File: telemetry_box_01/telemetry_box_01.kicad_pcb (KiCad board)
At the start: 4 copper layers, 86 x 44 mm, 103 parts, among them J1 78646-3001, J2 U.FL-R-SMT-1_10_, J3 U.FL-R-SMT-1_10_, J4 12401832E402A, U1 nRF52840, U2 A9G, U3 STBC08PMR, U4 TPS7A2633DRVR, Y1 Crystal_GND24, Y2 ABS04W-32.768KHZ-4-D2-T5

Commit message: fix(vias): blind vias have been removed to optimize production
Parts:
- C11, C12: value 0.8 -> 12
- C13, C14: value 0.8 -> 2
- R6, R7, R8, R9: value 1k -> 510
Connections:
- U1 pad A10: unconnected-(U1-AIN5/P0.29-PadA10) -> NRF_GPIO_01
- U1 pad A8: unconnected-(U1-AIN7/P0.31-PadA8) -> NRF_GPIO_02
- U1 pad AC15: unconnected-(U1-P0.19-PadAC15) -> NRF_RESET
- U1 pad AC17: unconnected-(U1-P0.21-PadAC17) -> NRF_RESET
- U1 pad AC19: unconnected-(U1-P0.23-PadAC19) -> NRF_RESET
- U1 pad AC21: unconnected-(U1-P0.25-PadAC21) -> NRF_RESET
- U1 pad B11: NRF_GPIO_01 -> unconnected-(U1-AIN4/P0.28-PadB11)
- U1 pad B9: NRF_GPIO_02 -> unconnected-(U1-AIN6/P0.30-PadB9)
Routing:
- net NRF_RESET: track 28.2 -> 29.8 mm, vias 4 -> 3
- net NRF_GPIO_02: track 9.54 -> 9.11 mm, vias 3 -> 2
- net NRF_GPIO_01: track 13.6 -> 13.2 mm, vias 3 -> 2

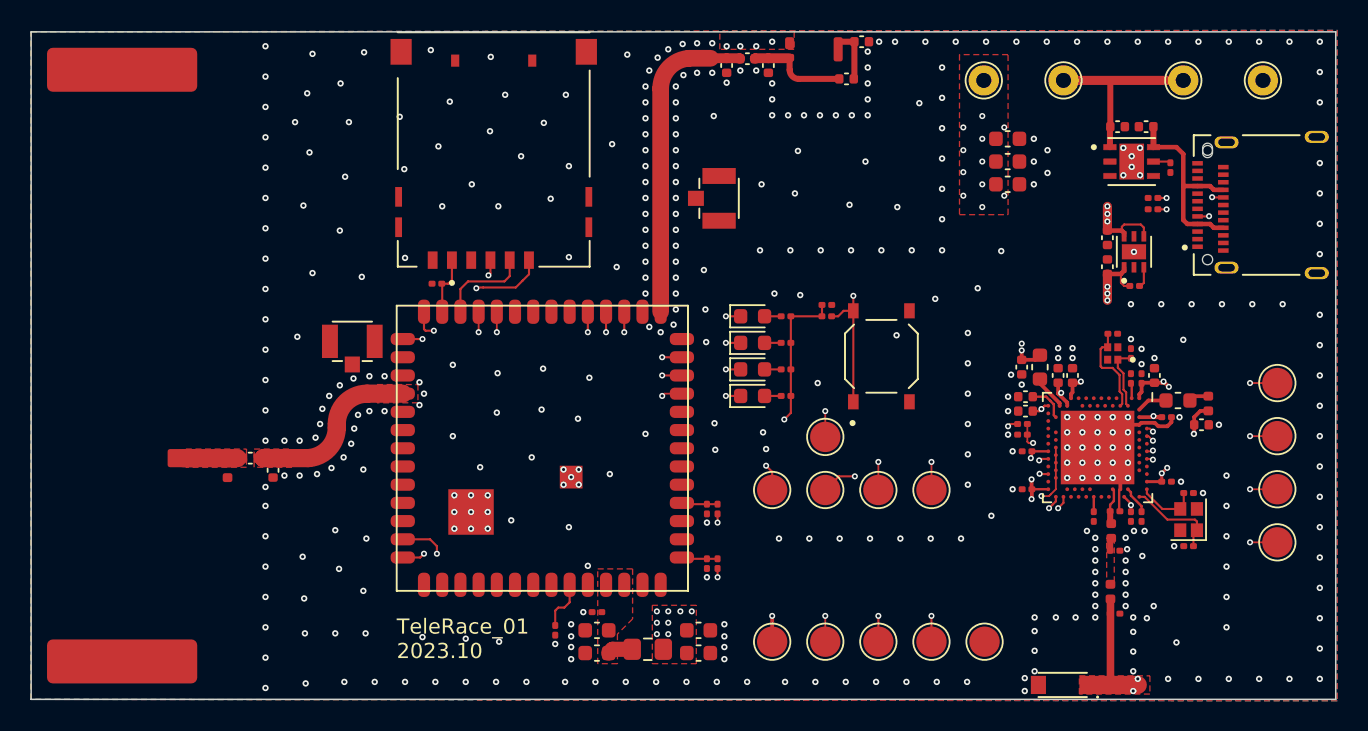
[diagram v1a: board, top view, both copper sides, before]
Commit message: feat(board): optimization of component placement -reduce product dimensions -remove GPS antenna -add power to the SMA connector for external GPS antenna -move debug pins -replace ble smd antenna with pсb antenna
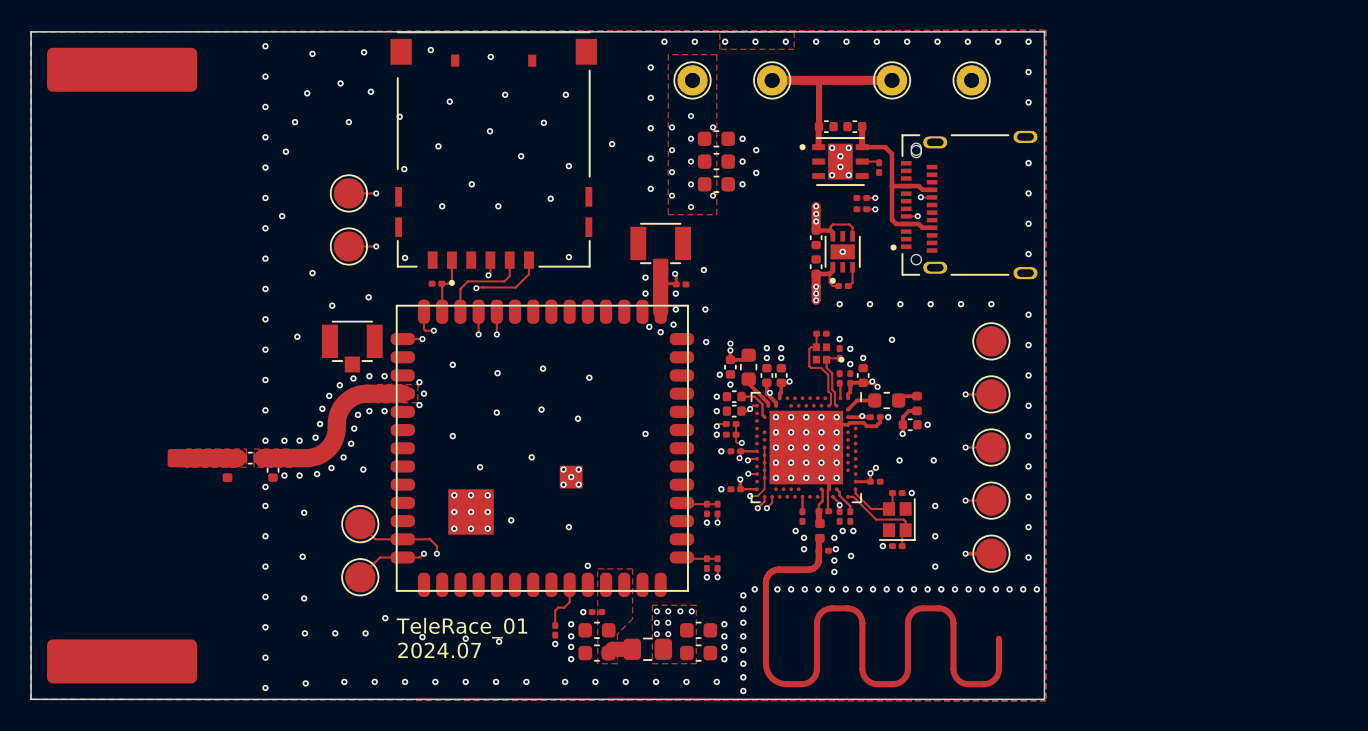
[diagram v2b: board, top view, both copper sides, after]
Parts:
- removed A1: GGBLA.01.A, RF:GGBLA.01.A
- removed AE1: AH316M245001-T, AH316M245001-T:XDCR_AH316M245001-T
- removed C31: 22, Capacitor_SMD:C_0402_1005Metric
- removed C32: 0.5, Capacitor_SMD:C_0402_1005Metric
- removed C33: 0.8, Capacitor_SMD:C_0402_1005Metric
- removed C34: 2.7, Capacitor_SMD:C_0402_1005Metric
- removed C35: NC, Capacitor_SMD:C_0402_1005Metric
- removed C40: 1, Capacitor_SMD:C_0201_0603Metric
- removed D1, D2, D3, D4: LED, LED_SMD:LED_0603_1608Metric
- removed L7: 3.6nH, Inductor_SMD:L_0402_1005Metric
- removed R5: 10k, Resistor_SMD:R_0201_0603Metric
- removed R6, R7, R8, R9: 510, Resistor_SMD:R_0201_0603Metric
- removed S1: PTS526_SM08_SMTR2_LFS, PTS526_SM08_SMTR2_LFS:SW_PTS526_SM08_SMTR2_LFS
- removed TP10: NRF_GPIO_03, TestPoint:TestPoint_Pad_D2.0mm
- removed TP11: NRF_GPIO_04, TestPoint:TestPoint_Pad_D2.0mm
- removed TP12: A9G_GPIO_01, TestPoint:TestPoint_Pad_D2.0mm
- removed TP8: NRF_GPIO_01, TestPoint:TestPoint_Pad_D2.0mm
- removed TP9: NRF_GPIO_02, TestPoint:TestPoint_Pad_D2.0mm
- moved TP14 43.1 mm to (121.0, 70.7), turned to 90 degrees
- moved TP13 38.4 mm to (121.0, 74.2), turned to 90 degrees
- moved TP7 30.7 mm to (121.7, 92.5), turned to 90 degrees
- moved TP6 27.8 mm to (121.7, 96.0), turned to 90 degrees
- moved TP5 19.8 mm to (163.3, 80.4), turned to 90 degrees
- moved C11 19.2 mm to (157.1, 93.9)
- moved C12 19.2 mm to (157.1, 90.4)
- moved C13 19.2 mm to (152.1, 79.9)
- moved C16 19.2 mm to (157.9, 85.9)
- moved C19 19.2 mm to (150.8, 92.0)
- moved C20 19.2 mm to (146.3, 84.0)
- moved C21 19.2 mm to (154.8, 82.7)
- moved C23 19.2 mm to (149.4, 82.7)
- moved C24 19.2 mm to (146.4, 87.7)
- moved C25 19.2 mm to (146.4, 90.2)
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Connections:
- J3 pad 2: unconnected-(J3-Pad2) -> A9G_GPS_ANT
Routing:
- net Net-(C10-Pad1): track 0.84 -> 50.8 mm
- net BTN_U2: track 34.6 -> 0.00 mm, vias 2 -> 0
- net A9G_LED_1: track 20.1 -> 0.00 mm, vias 2 -> 0
- net HST_RXD: track 35.4 -> 16.7 mm
- net NRF_TX: track 49.4 -> 30.9 mm, vias 3 -> 2
- net A9G_GPS_ANT: track 21.0 -> 2.95 mm
- net HST_TXD: track 37.6 -> 19.8 mm
- net NRF_RX: track 48.5 -> 30.8 mm, vias 3 -> 2
- net NRF_GPIO_04: track 14.7 -> 0.00 mm, vias 2 -> 0
- net A9G_GPIO_01: track 14.5 -> 0.00 mm, vias 2 -> 0
- net NRF_GPIO_01: track 13.2 -> 0.00 mm, vias 2 -> 0
- net NRF_SWDCLK: track 14.4 -> 27.4 mm
- net A9G_LED_4: track 12.8 -> 0.00 mm, vias 2 -> 0
- net +4V: track 74.7 -> 62.3 mm
- net NRF_GPIO_03: track 10.8 -> 0.00 mm, vias 2 -> 0
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- removed copper zone on F.Cu, net Net-(C10-Pad1)
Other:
- board size 86 x 44 mm -> 66.8 x 44 mm
- board text added: "TeleRace_01 2024.07"
- board text removed: "TeleRace_01 2023.10"

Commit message: feat(board): installation GPS antenna, power switch, tag-connect on PCB
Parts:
- removed J2, J3: U.FL-R-SMT-1_10_, U.FL-R-SMT-1_10_:HRS_U.FL-R-SMT-1_10_
- removed TP1: +3.3v, TestPoint:TestPoint_Pad_D2.0mm
- removed TP13: A9G_UART_HST_RX, TestPoint:TestPoint_Pad_D2.0mm
- removed TP14: A9G_UART_HST_TX, TestPoint:TestPoint_Pad_D2.0mm
- removed TP17, TP18: SWITCH_BATT+, TestPoint:TestPoint_THTPad_D2.0mm_Drill1.0mm
- removed TP2: reset, TestPoint:TestPoint_Pad_D2.0mm
- removed TP3: swdio, TestPoint:TestPoint_Pad_D2.0mm
- removed TP4: swclk, TestPoint:TestPoint_Pad_D2.0mm
- removed TP5: gnd, TestPoint:TestPoint_Pad_D2.0mm
- added C31: 0.1u, Capacitor_SMD:C_0201_0603Metric, F.Cu at (142.3, 76.8)
- added C32: 47, Capacitor_SMD:C_0201_0603Metric, F.Cu at (144.4, 78.3)
- added J5: TC2050-IDC, TAG_CONNECT_2050:CONN_TC2050-IDC_TGC, F.Cu at (161.0, 79.6)
- added J6: TC2050-IDC, TAG_CONNECT_2050:CONN_TC2050-IDC_TGC, F.Cu at (121.1, 72.0)
- added S1: SLW-108645-4A-RA-D, SLW-108645-4A-RA-D:SW_SLW-108645-4A-RA-D, F.Cu at (163.4, 90.9)
- added U5: SGGP.12.4.A.02, SGGP.12.4.A.02:SGGP.12.4.A.02, F.Cu at (144.0, 68.7)
- added U6: BGU8019, BGU8019:SOT1232, F.Cu at (144.0, 76.8)
- added U7: ADP150ACBZ-2.8-R7, ADP150ACBZ-2.8-R7:CB_4_3_ADI, F.Cu at (141.1, 76.8)
- moved C44 22.8 mm to (163.8, 83.1), turned to 90 degrees
- moved C45 22.5 mm to (162.3, 83.1), turned to 90 degrees
- moved C46 22.4 mm to (160.8, 83.1), turned to 90 degrees
- moved C42 7.44 mm to (147.4, 79.6), turned to 0 degrees
- moved U4 6.17 mm to (148.3, 77.8), turned to 180 degrees
- moved C43 4.79 mm to (149.3, 79.6), turned to 180 degrees
- moved R11 3.16 mm to (150.6, 77.8), turned to -90 degrees
- moved C41 2.98 mm to (139.9, 76.8), turned to 90 degrees
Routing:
- net +4V: track 62.3 -> 86.7 mm, vias 25 -> 15
- net +BATT: track 12.3 -> 36.5 mm
- net +3.3V: track 70.8 -> 58.1 mm
- net NRF_RESET: track 27.7 -> 36.0 mm
- net +2.8V: track 0.00 -> 6.26 mm
- net HST_RXD: track 16.7 -> 20.5 mm
- net NRF_SWDCLK: track 27.4 -> 24.3 mm
- net A9G_GPS_ANT: track 2.95 -> 5.31 mm, vias 0 -> 1
- net HST_TXD: track 19.8 -> 21.9 mm
- net Net-(U5-8): track 0.00 -> 1.90 mm
- net Net-(C32-Pad1): track 0.00 -> 0.98 mm
- net GND: vias 292 -> 297
- added copper zone on In1.Cu, net +BATT
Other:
- board text added: "TeleRace_01 2025.03"
- board text added: "Посмотреть землю на стабилизатор усилителя gps Убрать удаление маски на антенне gps, стабилизаторе, тумблере +Добавить стабилизатор напряжения на 2.8 вольт Провести ЮСБ для nrf с нулевыми резисторами +Добавить чип усилителя gps +тумблер включения таг-коннект для nrf +gps-антенна на плате (с усилителем) -световой индикатор -подвинуть a9g -слот под nano-sim таг-коннект для a9g"
- board text removed: "TeleRace_01 2024.07"
